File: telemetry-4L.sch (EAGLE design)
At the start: 72 parts, among them SW1 MF-SW-TACT-4.2MM, SW2 PCM12SMTR, U1 ATSAMD21G18A-MUT, U2 SPX3819M5-L-3-0, U3 MCP73831T-2ACI/OT, U4 IRLML6344TRPBF, U5 SIM868, U6 BMP280, U7 MPU-9250, U8 TPS61253YFFR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

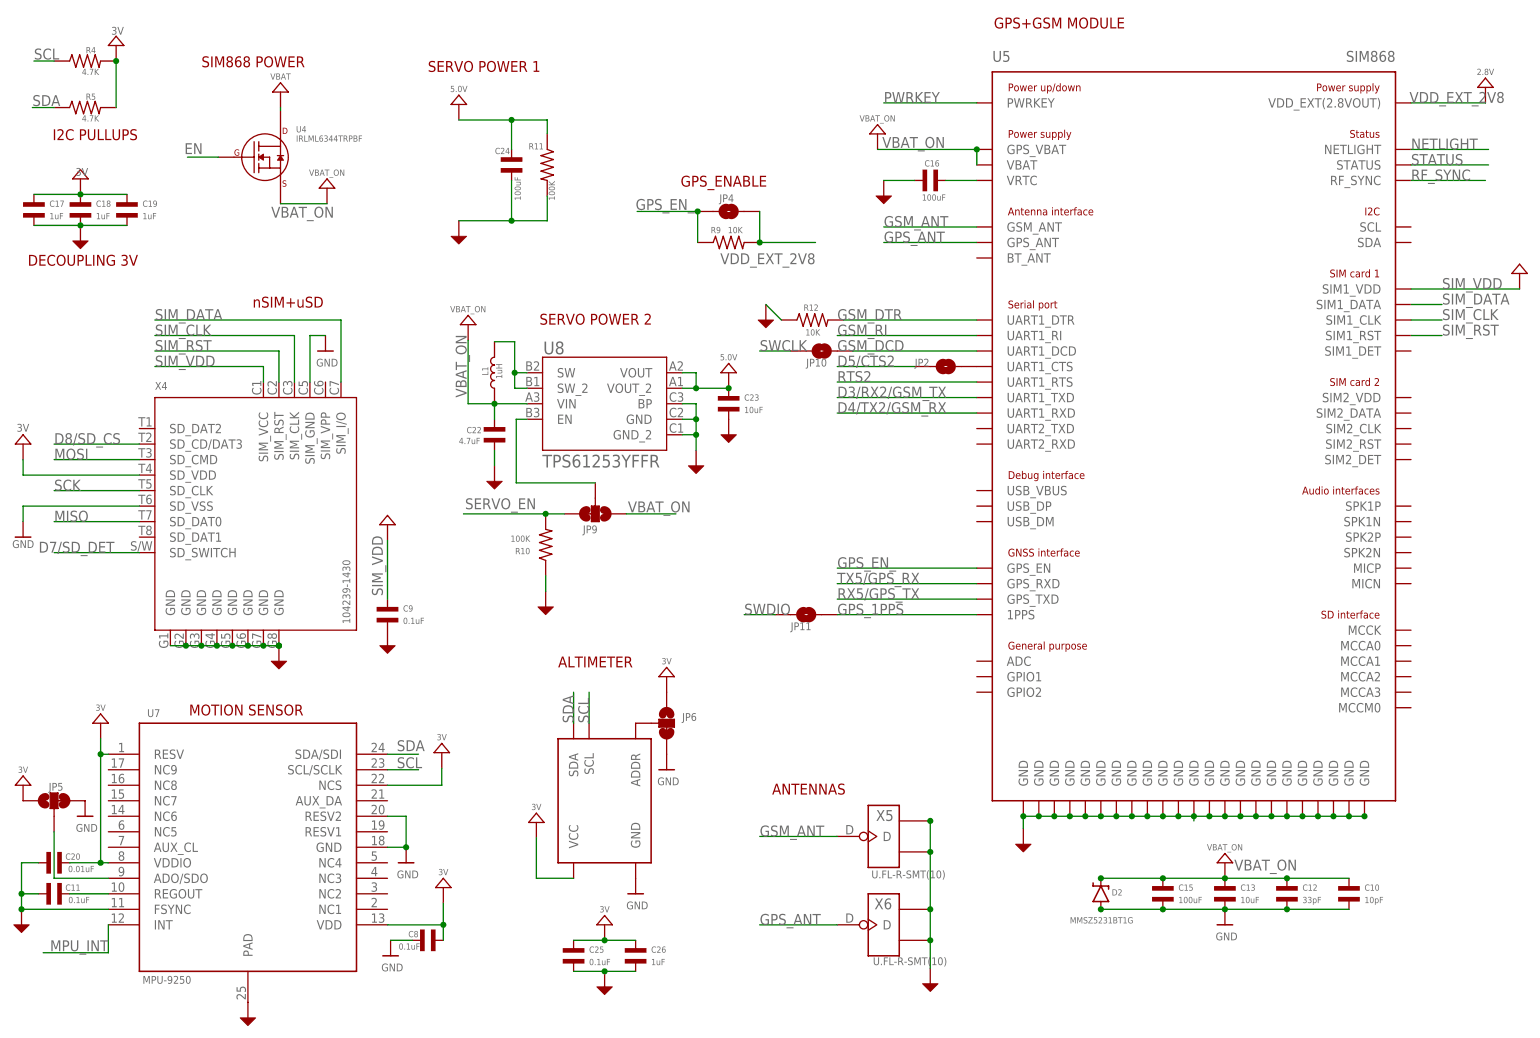
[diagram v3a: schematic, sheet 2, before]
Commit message: fixed more margins Remember: Have a look at A5 trace and via
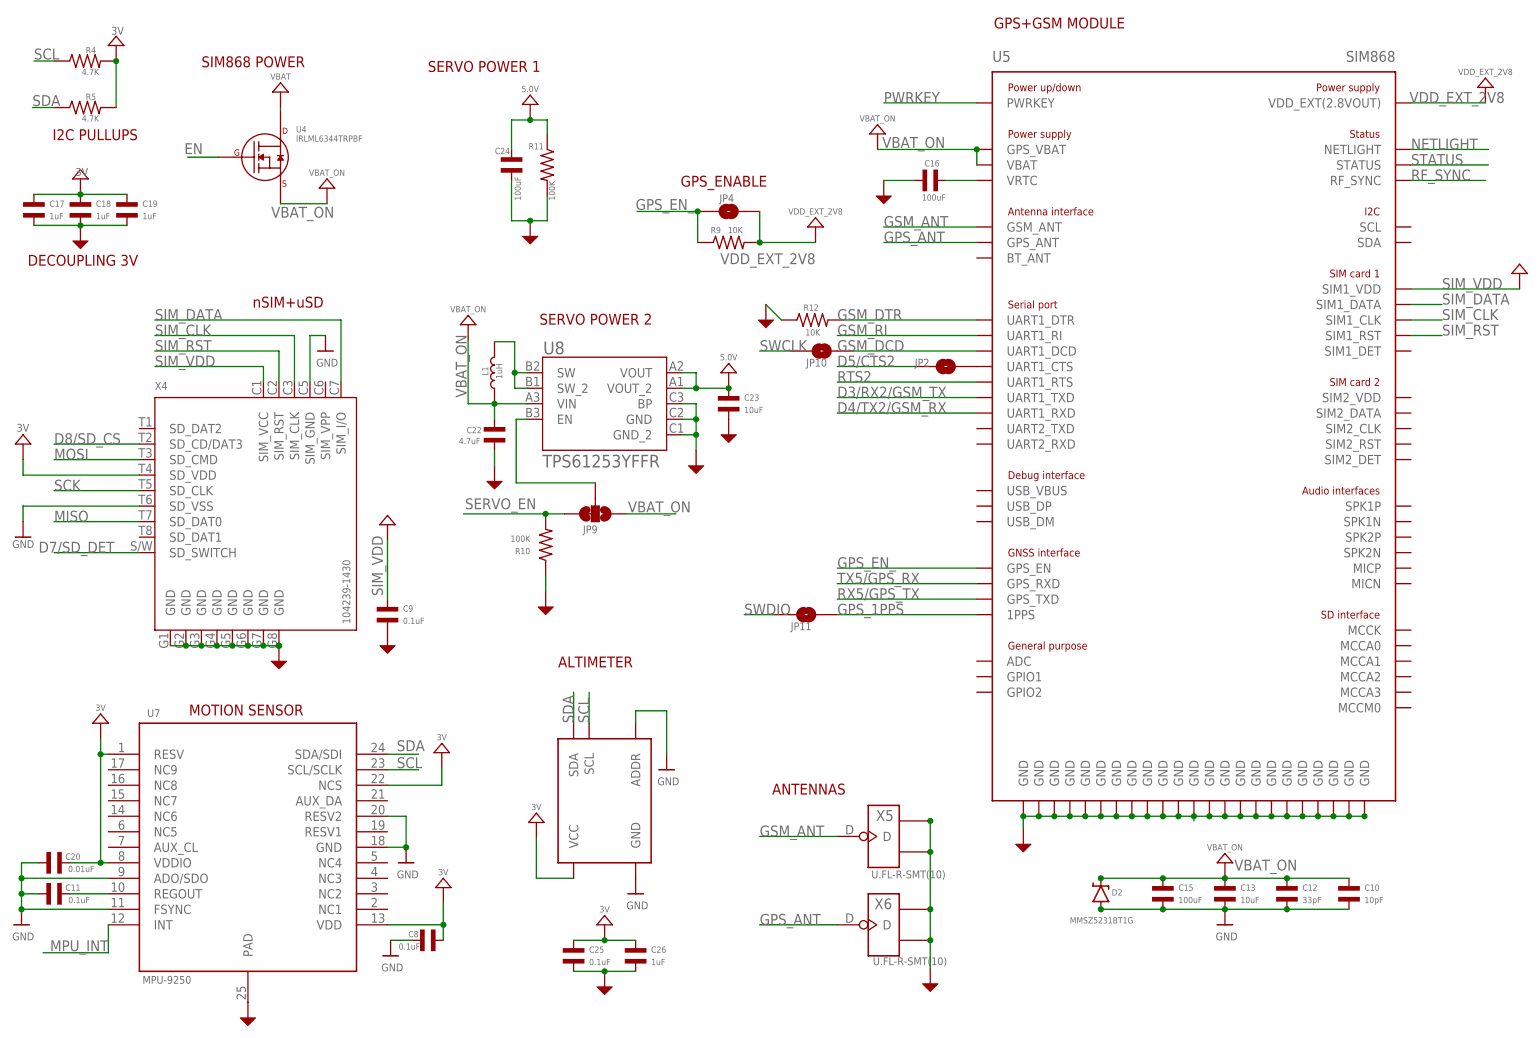
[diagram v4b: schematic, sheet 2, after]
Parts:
- removed JP5, JP6: JUMPER-PAD-3-2OF3_NC_BY_TRACE_SMALL, SparkFun-Passives:JUMPER-PAD-3-2OF3_NC_BY_TRACE_SMALL
- removed SW1: MF-SW-TACT-4.2MM, MF_Switches:TACT_4.2MM
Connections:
- removed net N$10: JP6.2, U6.ADDR
- removed net N$2: JP5.2, U7.ADO/SDO
- net !RESET: no longer SW1.P$1, SW1.P$2
- net +3V: no longer JP5.1, JP6.1
- net GND: now also U6.ADDR, U7.ADO/SDO; no longer JP5.3, JP6.3, SW1.P$3, SW1.P$4

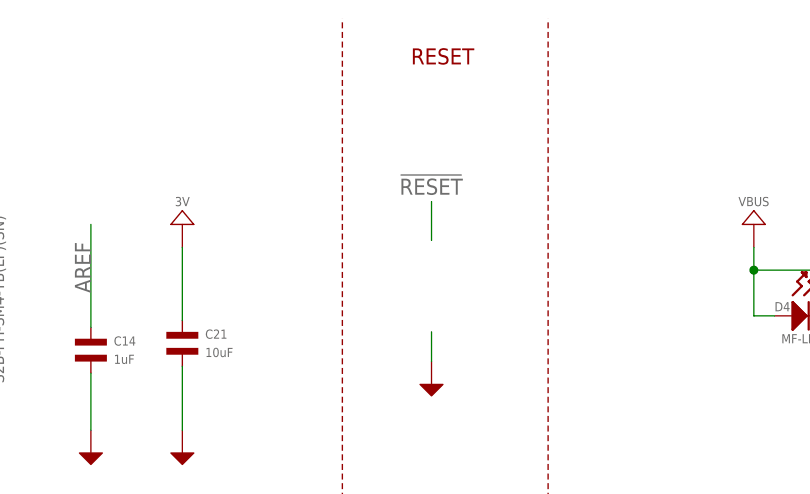
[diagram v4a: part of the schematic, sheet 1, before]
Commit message: moved sd slot to the left, making more room for a5
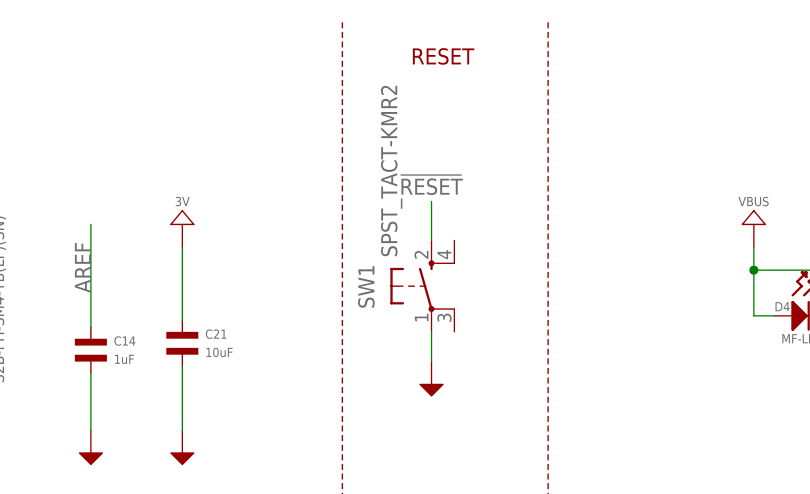
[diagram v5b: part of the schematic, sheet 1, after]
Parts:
- added SW1: SPST_TACT-KMR2, adafruit:SPST_TACT-KMR2
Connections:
- net !RESET: now also SW1.S
- net GND: now also SW1.P
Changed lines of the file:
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@@
 <part name="VDD_EXT_2V8" library="MF_Aesthetics" deviceset="POWER_RAIL" device="" value="VDD_EXT_2V8"/>
 <part name="VDD_EXT_2V1" library="MF_Aesthetics" deviceset="POWER_RAIL" device="" value="VDD_EXT_2V8"/>
+<part name="SW1" library="adafruit" deviceset="SPST_TACT" device="-KMR2"/>
 </parts>
 <sheets>
@@
 <instance part="JP3" gate="G$1" x="180.34" y="66.04"/>
 <instance part="5.0V" gate="G$1" x="147.32" y="50.8" rot="R90"/>
+<instance part="SW1" gate="G$1" x="121.666" y="145.542"/>
 </instances>
 <busses>
@@
 <wire x1="121.666" y1="140.462" x2="121.666" y2="137.16" width="0.1524" layer="91"/>
 <pinref part="U$47" gate="G$1" pin="P$1"/>
+<pinref part="SW1" gate="G$1" pin="P"/>
 </segment>
 <segment>
@@
 <label x="118.11" y="155.702" size="1.778" layer="95"/>
 <wire x1="121.666" y1="154.94" x2="121.666" y2="150.622" width="0.1524" layer="91"/>
-</segment>
-<segment>
+<pinref part="SW1" gate="G$1" pin="S"/>
+</segment>
+<segment>

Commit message: small fixes (some very important)
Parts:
- SW1: value SPST_TACT-KMR2 -> MF-SW-TACT-4.2MM; device adafruit:SPST_TACT-KMR2 -> MF_Switches:TACT_4.2MM
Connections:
- net !RESET: now also SW1.P$1, SW1.P$2; no longer SW1.S
- net GND: now also SW1.P$4; no longer SW1.P
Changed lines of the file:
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@@
 <part name="VDD_EXT_2V8" library="MF_Aesthetics" deviceset="POWER_RAIL" device="" value="VDD_EXT_2V8"/>
 <part name="VDD_EXT_2V1" library="MF_Aesthetics" deviceset="POWER_RAIL" device="" value="VDD_EXT_2V8"/>
-<part name="SW1" library="adafruit" deviceset="SPST_TACT" device="-KMR2"/>
+<part name="SW1" library="MF_Switches" deviceset="TACT" device="_4.2MM" value="MF-SW-TACT-4.2MM"/>
 </parts>
 <sheets>
@@
 <instance part="JP3" gate="G$1" x="180.34" y="66.04"/>
 <instance part="5.0V" gate="G$1" x="147.32" y="50.8" rot="R90"/>
-<instance part="SW1" gate="G$1" x="121.666" y="145.542"/>
+<instance part="SW1" gate="G$1" x="124.206" y="144.526"/>
 </instances>
 <busses>
@@
 </segment>
 <segment>
-<wire x1="121.666" y1="140.462" x2="121.666" y2="137.16" width="0.1524" layer="91"/>
 <pinref part="U$47" gate="G$1" pin="P$1"/>
-<pinref part="SW1" gate="G$1" pin="P"/>
+<pinref part="SW1" gate="G$1" pin="P$4"/>
+<wire x1="121.666" y1="139.7" x2="121.666" y2="137.16" width="0.1524" layer="91"/>
+<wire x1="126.746" y1="141.986" x2="126.746" y2="139.7" width="0.1524" layer="91"/>
+<wire x1="126.746" y1="139.7" x2="121.666" y2="139.7" width="0.1524" layer="91"/>
 </segment>
 <segment>
@@
 <segment>
 <label x="118.11" y="155.702" size="1.778" layer="95"/>
-<wire x1="121.666" y1="154.94" x2="121.666" y2="150.622" width="0.1524" layer="91"/>
-<pinref part="SW1" gate="G$1" pin="S"/>
-</segment>
-<segment>
+<wire x1="121.666" y1="154.94" x2="121.666" y2="148.59" width="0.1524" layer="91"/>
+<pinref part="SW1" gate="G$1" pin="P$2"/>
+<wire x1="126.746" y1="147.066" x2="126.746" y2="148.59" width="0.1524" layer="91"/>
+<wire x1="126.746" y1="148.59" x2="121.666" y2="148.59" width="0.1524" layer="91"/>
+<pinref part="SW1" gate="G$1" pin="P$1"/>
+<wire x1="121.666" y1="147.066" x2="121.666" y2="148.59" width="0.1524" layer="91"/>
+<junction x="121.666" y="148.59"/>
+</segment>
+<segment>
